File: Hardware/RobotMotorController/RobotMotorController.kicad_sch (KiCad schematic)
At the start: 12 parts, among them J1 PinSocket_2x16_P2.54mm_Vertic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, J10 CONN_01x04, J2 PinSocket_2x24_P2.54mm_Vertic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, J3 PinSocket_2x24_P2.54mm_Vertic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, J5 CONN_01x04, J7 CONN_01x04, J8 CONN_01x04, J9 CONN_01x04

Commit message: varius improvement
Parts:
- J2, J3: now in the parts list
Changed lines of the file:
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@@
   )
   (symbol (lib_id "Connector_Generic:Conn_02x24_Odd_Even") (at 142.24 48.26 0) (unit 1)
-    (in_bom no) (on_board yes)
+    (in_bom yes) (on_board yes)
     (property "Reference" "J3" (id 0) (at 143.51 15.3502 0))
     (property "Value" "PinSocket_2x24_P2.54mm_Vertical" (id 1) (at 143.51 17.8871 0))
@@
   )
   (symbol (lib_id "Connector_Generic:Conn_02x24_Odd_Even") (at 50.8 48.26 0) (unit 1)
-    (in_bom no) (on_board yes) (fields_autoplaced)
+    (in_bom yes) (on_board yes) (fields_autoplaced)
     (property "Reference" "J2" (id 0) (at 52.07 15.3502 0))
     (property "Value" "PinSocket_2x24_P2.54mm_Vertical" (id 1) (at 52.07 17.8871 0))

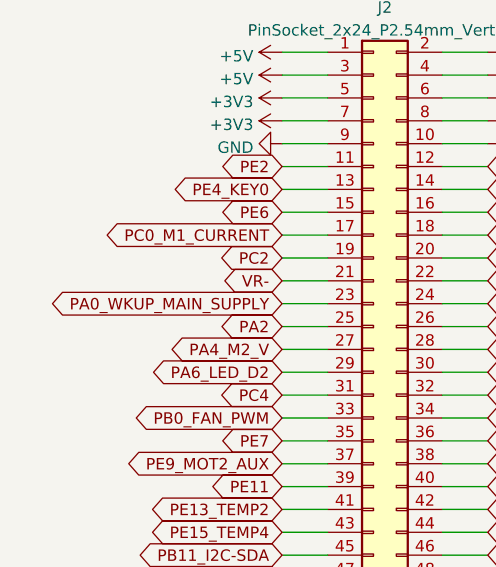
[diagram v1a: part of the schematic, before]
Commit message: ADC init completed
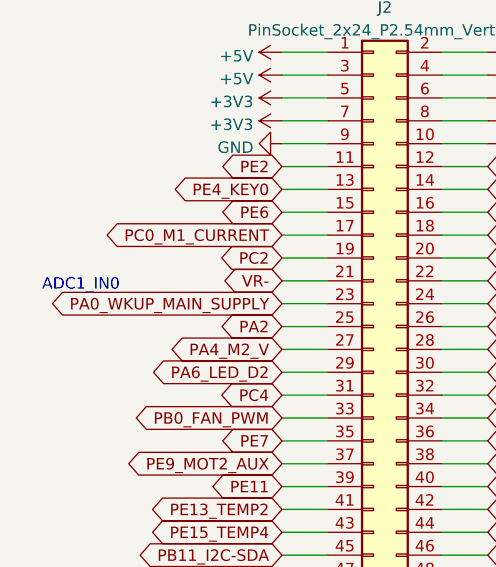
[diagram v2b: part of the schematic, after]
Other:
- note added: "ADC1_IN0"
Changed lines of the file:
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@@
     )
+  )
+  (text "ADC1_IN0" (at 13.97 46.99 0)
+    (effects (font (size 1.27 1.27)) (justify left bottom))
   )
   (label "PA9_E1_CHB" (at 203.2 76.2 0)

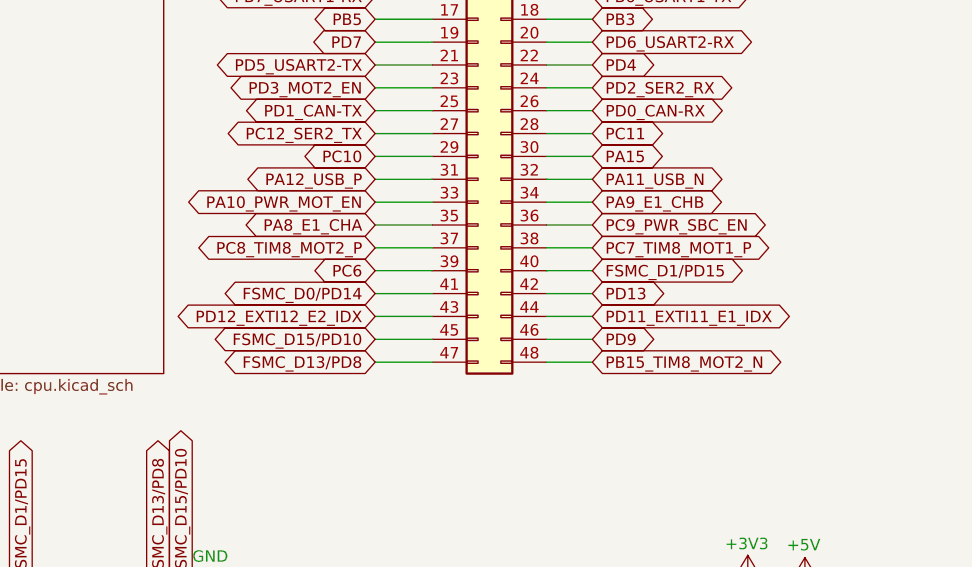
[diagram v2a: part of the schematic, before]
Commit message: General update, first encoder implementation
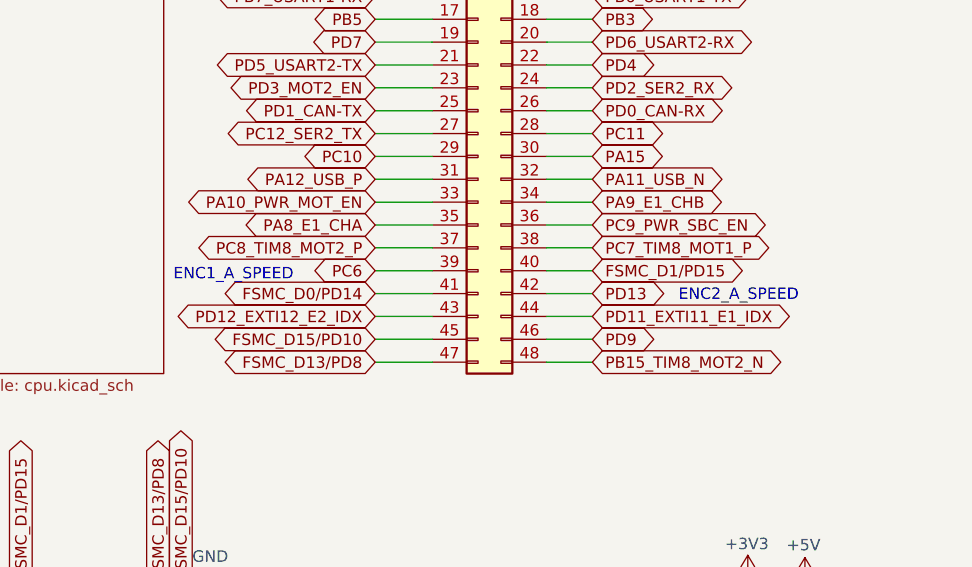
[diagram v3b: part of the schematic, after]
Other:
- note added: "ENC1_A_SPEED"
- note added: "ENC2_A_SPEED"
